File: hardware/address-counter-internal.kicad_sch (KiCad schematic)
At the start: 10 parts, among them U10 SN74LV163ADR, U11 SN74LV163ADR, U12 SN74LV163ADR, U13 SN74LV163ADR, U9 SN74LV163ADR

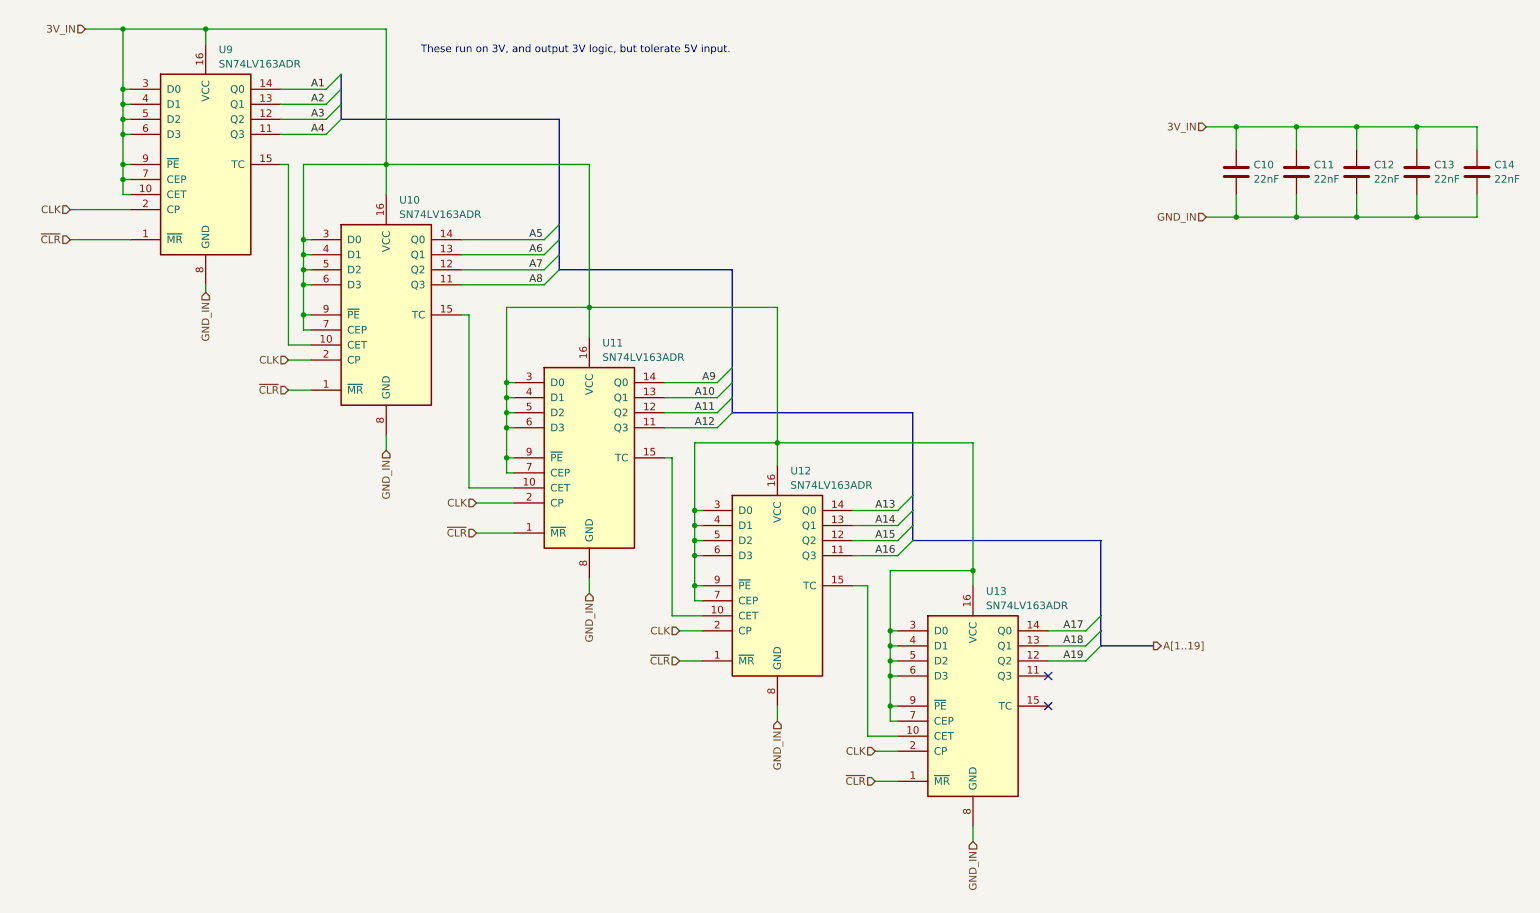
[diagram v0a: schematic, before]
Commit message: Massively reorganize board designs
Now planning to have most assembly done by JLCPCB, so trace sizes,
part selections, etc. are set accordingly.

New boards are:
 - cartridge interface & flash
 - microcontroller & registers
 - sram x2
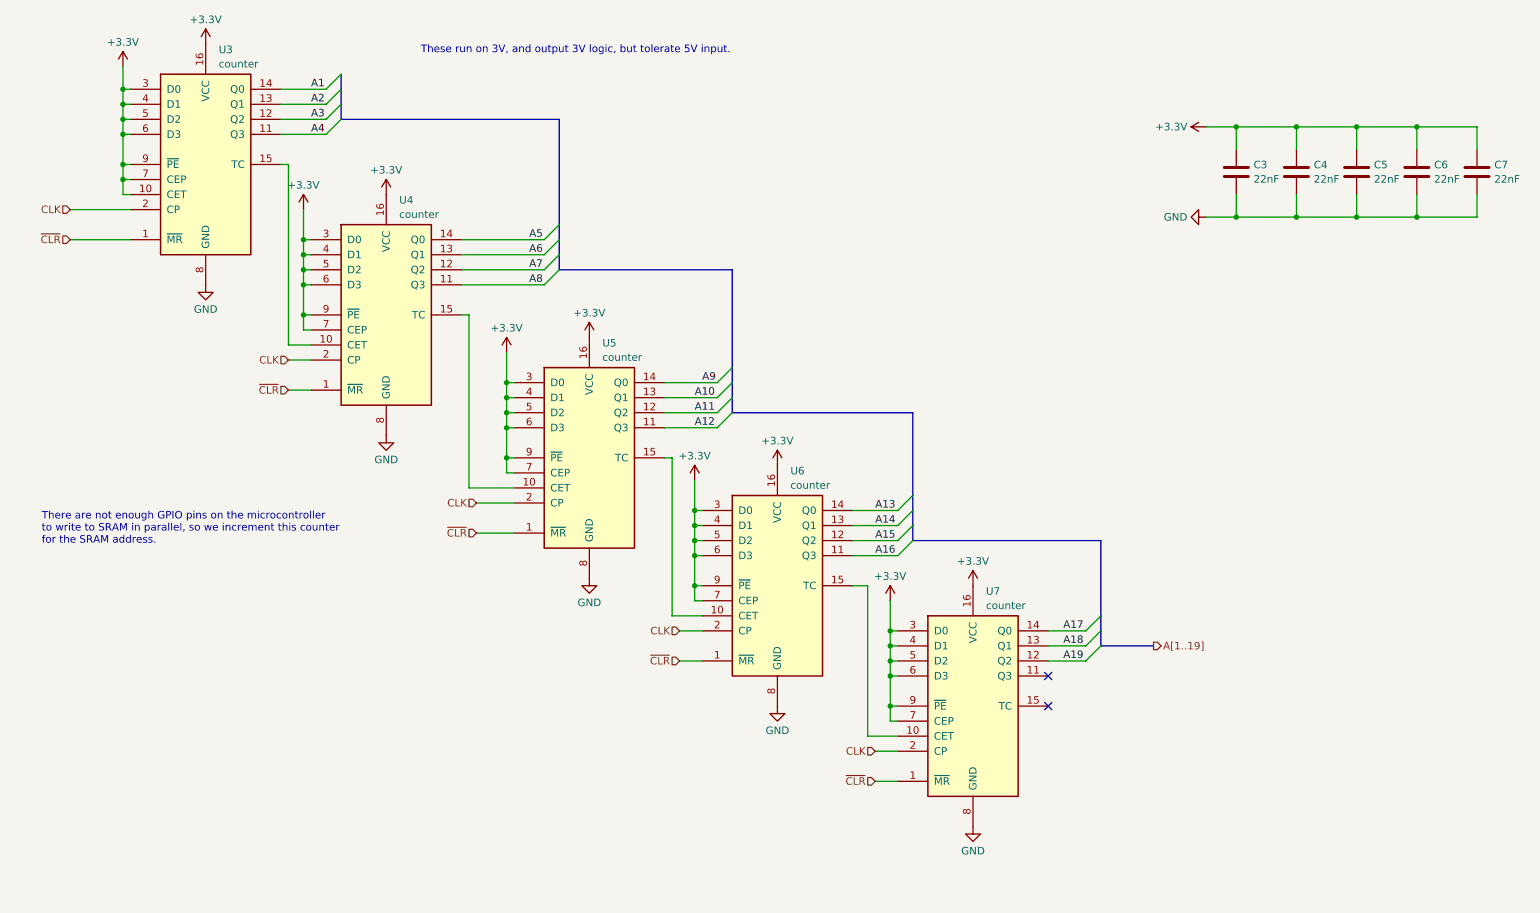
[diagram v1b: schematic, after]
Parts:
- C3: renamed from C10; JLCPCB Part Number (none) -> C21122; Mouser Part Number (none) -> 187-CL10B223KB8NNNC; Part Number (none) -> CL10B223KB8NNNC
- C4: renamed from C11; JLCPCB Part Number (none) -> C21122; Mouser Part Number (none) -> 187-CL10B223KB8NNNC; Part Number (none) -> CL10B223KB8NNNC
- C5: renamed from C12; JLCPCB Part Number (none) -> C21122; Mouser Part Number (none) -> 187-CL10B223KB8NNNC; Part Number (none) -> CL10B223KB8NNNC
- C6: renamed from C13; JLCPCB Part Number (none) -> C21122; Mouser Part Number (none) -> 187-CL10B223KB8NNNC; Part Number (none) -> CL10B223KB8NNNC
- C7: renamed from C14; JLCPCB Part Number (none) -> C21122; Mouser Part Number (none) -> 187-CL10B223KB8NNNC; Part Number (none) -> CL10B223KB8NNNC
- U3: renamed from U9; value SN74LV163ADR -> counter; footprint Package_SO:SOIC-16_3.9x9.9mm_P1.27mm -> Package_SO:TSSOP-16_4.4x3.6mm_P0.4mm; JLCPCB Part Number (none) -> C2872908; Mouser Part Number (none) -> 595-SN74LV163ADGVR; Part Number (none) -> SN74LV163ADGVR
- U4: renamed from U10; value SN74LV163ADR -> counter; footprint Package_SO:SOIC-16_3.9x9.9mm_P1.27mm -> Package_SO:TSSOP-16_4.4x3.6mm_P0.4mm; JLCPCB Part Number (none) -> C2872908; Mouser Part Number (none) -> 595-SN74LV163ADGVR; Part Number (none) -> SN74LV163ADGVR
- U5: renamed from U11; value SN74LV163ADR -> counter; footprint Package_SO:SOIC-16_3.9x9.9mm_P1.27mm -> Package_SO:TSSOP-16_4.4x3.6mm_P0.4mm; JLCPCB Part Number (none) -> C2872908; Mouser Part Number (none) -> 595-SN74LV163ADGVR; Part Number (none) -> SN74LV163ADGVR
- U6: renamed from U12; value SN74LV163ADR -> counter; footprint Package_SO:SOIC-16_3.9x9.9mm_P1.27mm -> Package_SO:TSSOP-16_4.4x3.6mm_P0.4mm; JLCPCB Part Number (none) -> C2872908; Mouser Part Number (none) -> 595-SN74LV163ADGVR; Part Number (none) -> SN74LV163ADGVR
- U7: renamed from U13; value SN74LV163ADR -> counter; footprint Package_SO:SOIC-16_3.9x9.9mm_P1.27mm -> Package_SO:TSSOP-16_4.4x3.6mm_P0.4mm; JLCPCB Part Number (none) -> C2872908; Mouser Part Number (none) -> 595-SN74LV163ADGVR; Part Number (none) -> SN74LV163ADGVR
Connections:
- net 3V_IN renamed +3.3V
- net GND_IN renamed GND
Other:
- note added: "There are not enough GPIO pins on the microcontroller to write to SRAM in parallel, so we increment this counter for the SRAM address."

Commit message: Revise microcontroller board based on latest cart board improvements
 - Update comments
 - Segregate the Ethernet module's power supply so it can be
   disconnected if something goes wrong in a prototype
 - Update board setup to match latest cart board
 - Remove unnecessary level-shifter
 - Fix address decoder to non-latching version
 - Fix address decoder output assignment
 - Consolidate buffer ICs in register file
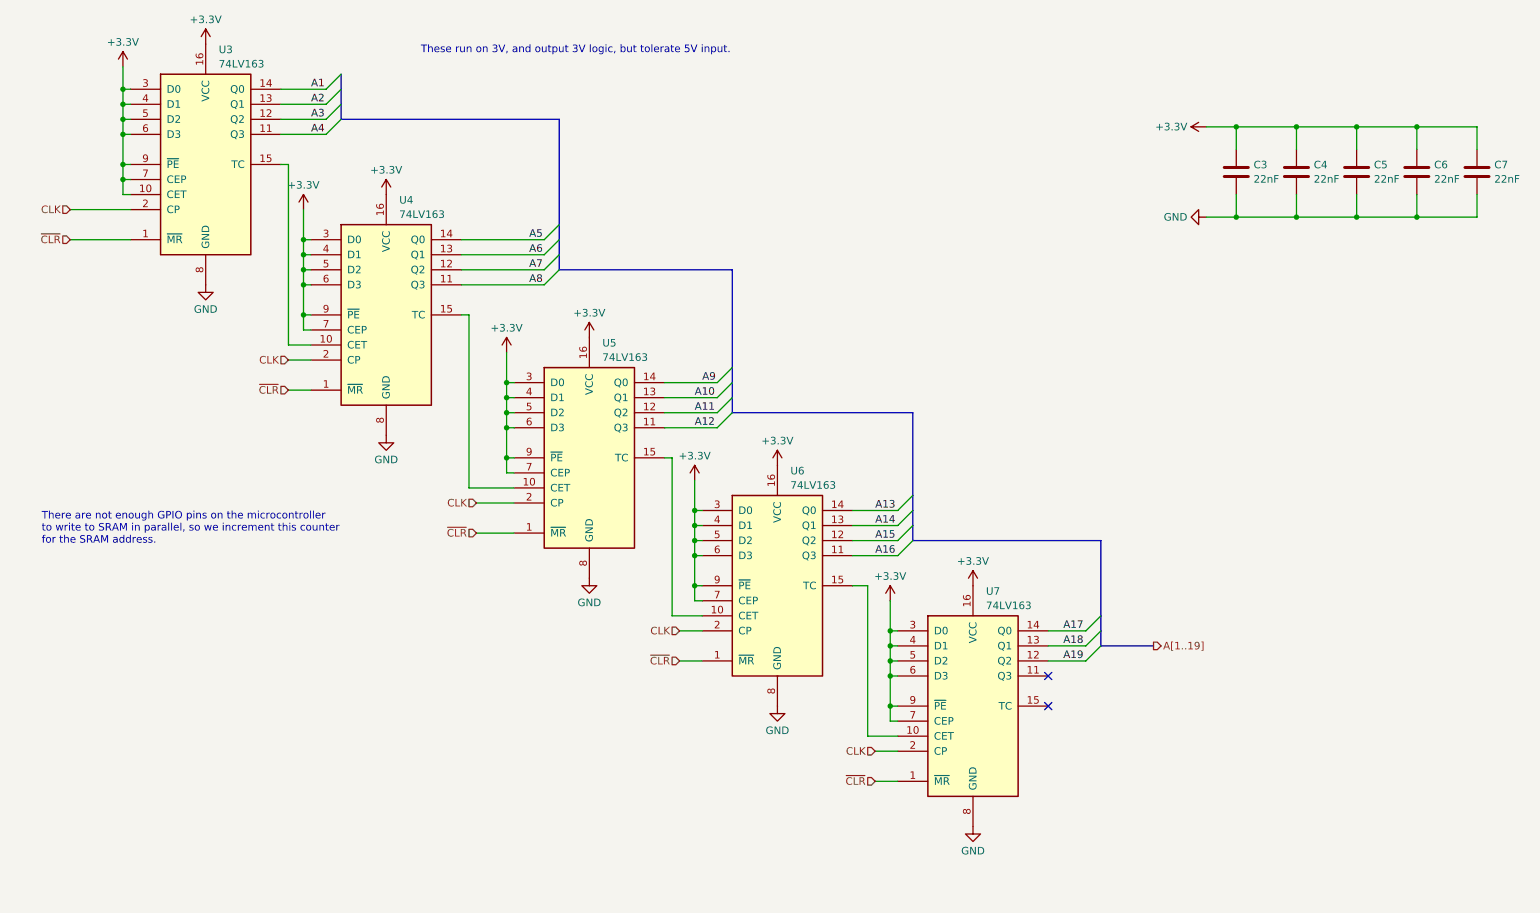
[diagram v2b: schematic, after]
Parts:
- U3, U4, U5, U6, U7: value counter -> 74LV163
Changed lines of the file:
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@@
 			)
 		)
-		(property "Value" "counter"
+		(property "Value" "74LV163"
 			(at 80.9341 50.3498 0)
 			(effects
@@
 			)
 		)
-		(property "Value" "counter"
+		(property "Value" "74LV163"
 			(at 146.9741 96.0698 0)
 			(effects
@@
 			)
 		)
-		(property "Value" "counter"
+		(property "Value" "74LV163"
 			(at 179.9941 116.3898 0)
 			(effects
@@
 			)
 		)
-		(property "Value" "counter"
+		(property "Value" "74LV163"
 			(at 50.4541 24.9498 0)
 			(effects
@@
 			)
 		)
-		(property "Value" "counter"
+		(property "Value" "74LV163"
 			(at 115.2241 74.4798 0)
 			(effects

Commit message: Replace address counters with slightly larger versions that can be assembled more easily
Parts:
- U3, U4, U5, U6, U7: footprint Package_SO:TSSOP-16_4.4x3.6mm_P0.4mm -> Package_SO:TSSOP-16_4.4x5mm_P0.65mm; JLCPCB Part Number C2872908 -> C2675453; Mouser Part Number 595-SN74LV163ADGVR -> 595-SN74LV163APWR; Part Number SN74LV163ADGVR -> SN74LV163APWR
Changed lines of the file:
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@@
 			)
 		)
-		(property "Footprint" "Package_SO:TSSOP-16_4.4x3.6mm_P0.4mm"
+		(property "Footprint" "Package_SO:TSSOP-16_4.4x5mm_P0.65mm"
 			(at 78.74 67.31 0)
 			(effects
@@
 			)
 		)
-		(property "Mouser Part Number" "595-SN74LV163ADGVR"
+		(property "Mouser Part Number" "595-SN74LV163APWR"
 			(at 78.74 67.31 0)
 			(effects
@@
 			)
 		)
-		(property "Part Number" "SN74LV163ADGVR"
+		(property "Part Number" "SN74LV163APWR"
 			(at 78.74 67.31 0)
 			(effects
@@
 			)
 		)
-		(property "JLCPCB Part Number" "C2872908"
+		(property "JLCPCB Part Number" "C2675453"
 			(at 78.74 67.31 0)
 			(effects
@@
 			)
 		)
-		(property "Footprint" "Package_SO:TSSOP-16_4.4x3.6mm_P0.4mm"
+		(property "Footprint" "Package_SO:TSSOP-16_4.4x5mm_P0.65mm"
 			(at 144.78 113.03 0)
 			(effects
@@
 			)
 		)
-		(property "Mouser Part Number" "595-SN74LV163ADGVR"
+		(property "Mouser Part Number" "595-SN74LV163APWR"
 			(at 144.78 113.03 0)
 			(effects
@@
 			)
 		)
-		(property "Part Number" "SN74LV163ADGVR"
+		(property "Part Number" "SN74LV163APWR"
 			(at 144.78 113.03 0)
 			(effects
@@
 			)
 		)
-		(property "JLCPCB Part Number" "C2872908"
+		(property "JLCPCB Part Number" "C2675453"
 			(at 144.78 113.03 0)
 			(effects
@@
 			)
 		)
-		(property "Footprint" "Package_SO:TSSOP-16_4.4x3.6mm_P0.4mm"
+		(property "Footprint" "Package_SO:TSSOP-16_4.4x5mm_P0.65mm"
 			(at 177.8 133.35 0)
 			(effects
@@
 			)
 		)
-		(property "Mouser Part Number" "595-SN74LV163ADGVR"
+		(property "Mouser Part Number" "595-SN74LV163APWR"
 			(at 177.8 133.35 0)
 			(effects
@@
 			)
 		)
-		(property "Part Number" "SN74LV163ADGVR"
+		(property "Part Number" "SN74LV163APWR"
 			(at 177.8 133.35 0)
 			(effects
@@
 			)
 		)
-		(property "JLCPCB Part Number" "C2872908"
+		(property "JLCPCB Part Number" "C2675453"
 			(at 177.8 133.35 0)
 			(effects
@@
 			)
 		)
-		(property "Footprint" "Package_SO:TSSOP-16_4.4x3.6mm_P0.4mm"
+		(property "Footprint" "Package_SO:TSSOP-16_4.4x5mm_P0.65mm"
 			(at 48.26 41.91 0)
 			(effects
@@
 			)
 		)
-		(property "Mouser Part Number" "595-SN74LV163ADGVR"
+		(property "Mouser Part Number" "595-SN74LV163APWR"
 			(at 48.26 41.91 0)
 			(effects
@@
 			)
 		)
-		(property "Part Number" "SN74LV163ADGVR"
+		(property "Part Number" "SN74LV163APWR"
 			(at 48.26 41.91 0)
 			(effects
@@
 			)
 		)
-		(property "JLCPCB Part Number" "C2872908"
+		(property "JLCPCB Part Number" "C2675453"
 			(at 48.26 41.91 0)
 			(effects
@@
 			)
 		)
-		(property "Footprint" "Package_SO:TSSOP-16_4.4x3.6mm_P0.4mm"
+		(property "Footprint" "Package_SO:TSSOP-16_4.4x5mm_P0.65mm"
 			(at 113.03 91.44 0)
 			(effects
@@
 			)
 		)
-		(property "Mouser Part Number" "595-SN74LV163ADGVR"
+		(property "Mouser Part Number" "595-SN74LV163APWR"
 			(at 113.03 91.44 0)
 			(effects
@@
 			)
 		)
-		(property "Part Number" "SN74LV163ADGVR"
+		(property "Part Number" "SN74LV163APWR"
 			(at 113.03 91.44 0)
 			(effects
@@
 			)
 		)
-		(property "JLCPCB Part Number" "C2872908"
+		(property "JLCPCB Part Number" "C2675453"
 			(at 113.03 91.44 0)
 			(effects
